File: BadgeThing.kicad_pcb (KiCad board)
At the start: 2 copper layers, 78.7 x 40.2 mm, 66 parts, among them J2 Ext 5V, J3 External 3V3, J4 SWD Header, J5 USB_C_Receptacle_USB2.0, J6 Connector_Generic_Conn_01x02, J7 Conn_01x06, SW1 ESP RESET, SW2 Left, SW3 Down, SW4 Select, SW5 Up, SW6 Right, SW7 BOOTSEL, U1 ESP-12F, U3 RP2040, U4 NCP1117-3.3_SOT223, U5 W25Q32JVSS, U6 USBLC6-2SC6, Y1 12.000MHz

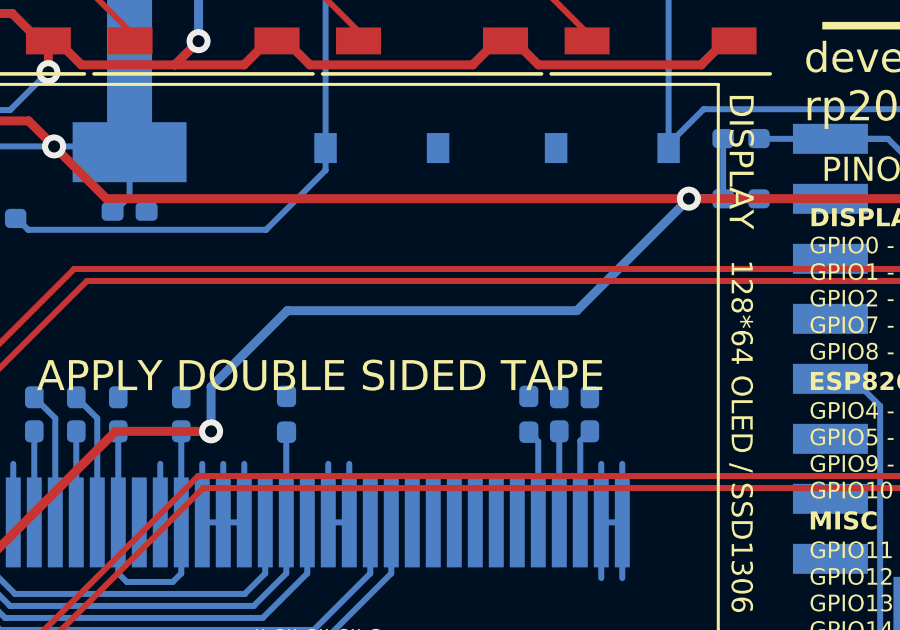
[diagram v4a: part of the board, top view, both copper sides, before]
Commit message: Update 3D models
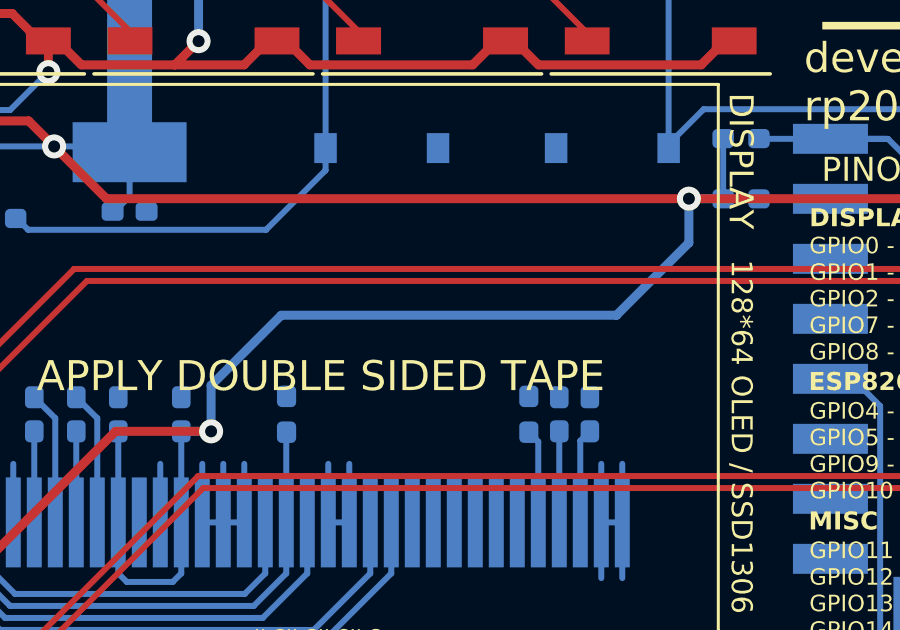
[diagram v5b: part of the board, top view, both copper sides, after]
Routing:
- net +3V3: track 196.5 -> 197.4 mm
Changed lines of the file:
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@@
     (property "ki_keywords" "switch normally-open pushbutton push-button")
     (attr smd)
-    (fp_text reference "SW1" (at -3.467 -0.0042 180) (layer "B.SilkS")
+    (fp_text reference "SW1" (at -3.467 -0.0042) (layer "B.SilkS")
         (effects (font (size 0.6 0.6) (thickness 0.15)) (justify mirror))
     )
@@
     (pad "2" smd rect (at 3 -1.875 270) (size 1 0.75) (layers "B.Cu" "B.Paste" "B.Mask")
       (net 54 "ESP_RST") (pinfunction "2") (pintype "passive"))
-    (model "${KICAD7_3DMODEL_DIR}/Button_Switch_SMD.3dshapes/SW_Push_1P1T_XKB_TS-1187A.wrl"
+    (model ":KICAD7_3DMODEL_DIR:Button_Switch_SMD.3dshapes/SW_SPST_TL3342.step"
       (offset (xyz 0 0 0))
       (scale (xyz 1 1 1))
@@
     (pad "8" smd roundrect (at 3.6 1.905 270) (size 1.6 0.6) (layers "B.Cu" "B.Paste" "B.Mask") (roundrect_rratio 0.25)
       (net 2 "+3V3") (pinfunction "VCC") (pintype "power_in"))
-    (model "${KICAD6_3DMODEL_DIR}/Package_SO.3dshapes/SOIC-8_5.23x5.23mm_P1.27mm.wrl"
+    (model ":KICAD7_3DMODEL_DIR:Package_SO.3dshapes/SOIC-8-1EP_3.9x4.9mm_P1.27mm_EP2.35x2.35mm.step"
+      (offset (xyz 0 0 0))
+      (scale (xyz 1 1 1))
+      (rotate (xyz 0 0 0))
+    )
+    (model ":KICAD7_3DMODEL_DIR:Package_SO.3dshapes/SOIC-8_5.275x5.275mm_P1.27mm.step"
       (offset (xyz 0 0 0))
       (scale (xyz 1 1 1))
@@
       (rotate (xyz 0 0 0))
     )
+    (model ":KICAD7_3DMODEL_DIR:Connector_USB.3dshapes/USB_C_Receptacle_GCT_USB4105-xx-A_16P_TopMnt_Horizontal.wrl"
+      (offset (xyz 0 0 0))
+      (scale (xyz 1 1 1))
+      (rotate (xyz 0 0 0))
+    )
   )
   (footprint "Capacitor_SMD:C_0402_1005Metric_Pad0.74x0.62mm_HandSolder" (layer "B.Cu")
@@
       (rotate (xyz 0 0 0))
     )
+    (model ":KICAD7_3DMODEL_DIR:Button_Switch_SMD.3dshapes/SW_SPST_TL3342.step"
+      (offset (xyz 0 0 0))
+      (scale (xyz 1 1 1))
+      (rotate (xyz 0 0 0))
+    )
   )
   (footprint "Capacitor_SMD:C_0402_1005Metric_Pad0.74x0.62mm_HandSolder" (layer "B.Cu")
@@
     (attr smd)
     (fp_text reference "U6" (at 0 2.4 90) (layer "B.SilkS")
-        (effects (font (size 1 1) (thickness 0.15)) (justify mirror))
+        (effects (font (size 0.8 0.8) (thickness 0.15)) (justify mirror))
     )
     (fp_text value "USBLC6-2SC6" (at 0 -2.4 90) (layer "B.Fab")
@@
   (via (at 158.1912 112.3275) (size 0.8) (drill 0.4) (layers "F.Cu" "B.Cu") (net 2))
   (segment (start 155.4734 104.4956) (end 155.4734 103.0228) (width 0.2) (layer "B.Cu") (net 2))
+  (segment (start 158.1912 110.7948) (end 158.1912 112.3275) (width 0.3) (layer "B.Cu") (net 2))
   (segment (start 136.992 111.846) (end 136.992 113.4025) (width 0.2) (layer "B.Cu") (net 2))
   (segment (start 135.387711 114.24) (end 135.7545 114.24) (width 0.2) (layer "B.Cu") (net 2))
   (segment (start 133.446604 110.274299) (end 133.446604 110.332604) (width 0.2) (layer "B.Cu") (net 2))
-  (segment (start 174.117 104.5718) (end 170.3832 108.3056) (width 0.3) (layer "B.Cu") (net 2))
   (segment (start 138.992 119.638) (end 139.11 119.52) (width 0.2) (layer "B.Cu") (net 2))
+  (segment (start 174.117 106.045) (end 171.704 108.458) (width 0.3) (layer "B.Cu") (net 2))
   (segment (start 150.4696 102.8313) (end 155.2819 102.8313) (width 0.2) (layer "B.Cu") (net 2))
   (segment (start 136.992 114.118) (end 136.87 114.24) (width 0.2) (layer "B.Cu") (net 2))
@@
   (segment (start 136.592 113.4025) (end 136.592 114.182) (width 0.2) (layer "B.Cu") (net 2))
   (segment (start 139.11 119.52) (end 139.11 119.33) (width 0.2) (layer "B.Cu") (net 2))
+  (segment (start 160.528 108.458) (end 158.1912 110.7948) (width 0.3) (layer "B.Cu") (net 2))
   (segment (start 142.6295 117.84) (end 141.91 117.84) (width 0.2) (layer "B.Cu") (net 2))
   (segment (start 156.9122 117.348) (end 157.1972 117.063) (width 0.2) (layer "B.Cu") (net 2))
@@
   (segment (start 155.4734 96.7228) (end 155.4734 103.0228) (width 1.5) (layer "B.Cu") (net 2))
   (segment (start 192.8296 128.0696) (end 194.041 129.281) (width 0.3) (layer "B.Cu") (net 2))
-  (segment (start 170.3832 108.3056) (end 160.7312 108.3056) (width 0.3) (layer "B.Cu") (net 2))
   (segment (start 155.3822 117.348) (end 156.9122 117.348) (width 0.2) (layer "B.Cu") (net 2))
   (segment (start 192.8296 117.7844) (end 192.8296 128.0696) (width 0.3) (layer "B.Cu") (net 2))
+  (segment (start 174.117 104.5718) (end 174.117 106.045) (width 0.3) (layer "B.Cu") (net 2))
   (segment (start 135.4836 110.274299) (end 135.4836 110.3376) (width 0.2) (layer "B.Cu") (net 2))
-  (segment (start 160.7312 108.3056) (end 158.1912 110.8456) (width 0.3) (layer "B.Cu") (net 2))
   (segment (start 194.036 116.578) (end 192.8296 117.7844) (width 0.3) (layer "B.Cu") (net 2))
   (segment (start 143.6074 103.4474) (end 143.08 102.92) (width 0.2) (layer "B.Cu") (net 2))
@@
   (segment (start 138.992 120.2775) (end 138.992 119.638) (width 0.2) (layer "B.Cu") (net 2))
   (segment (start 175.2526 104.5718) (end 175.2588 104.578) (width 0.3) (layer "B.Cu") (net 2))
-  (segment (start 158.1912 110.8456) (end 158.1912 112.3275) (width 0.3) (layer "B.Cu") (net 2))
   (segment (start 136.534 114.24) (end 135.7545 114.24) (width 0.2) (layer "B.Cu") (net 2))
   (segment (start 155.0972 115.363) (end 155.0972 117.063) (width 0.2) (layer "B.Cu") (net 2))
   (segment (start 137.392 121.286628) (end 136.15 122.528628) (width 0.2) (layer "B.Cu") (net 2))
+  (segment (start 171.704 108.458) (end 160.528 108.458) (width 0.3) (layer "B.Cu") (net 2))
   (segment (start 136.15 122.528628) (end 136.15 123.0525) (width 0.2) (layer "B.Cu") (net 2))
   (segment (start 139.39389 112.80611) (end 139.39389 111.41389) (width 0.2) (layer "F.Cu") (net 3))
